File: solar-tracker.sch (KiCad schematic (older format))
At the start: 21 parts, among them J1 LDR1, J2 LDR2, J3 Motor, J4 Power, Q1 TIP41C, Q2 TIP41C, Q3 TIP42C, Q4 TIP42C, U1 LM324

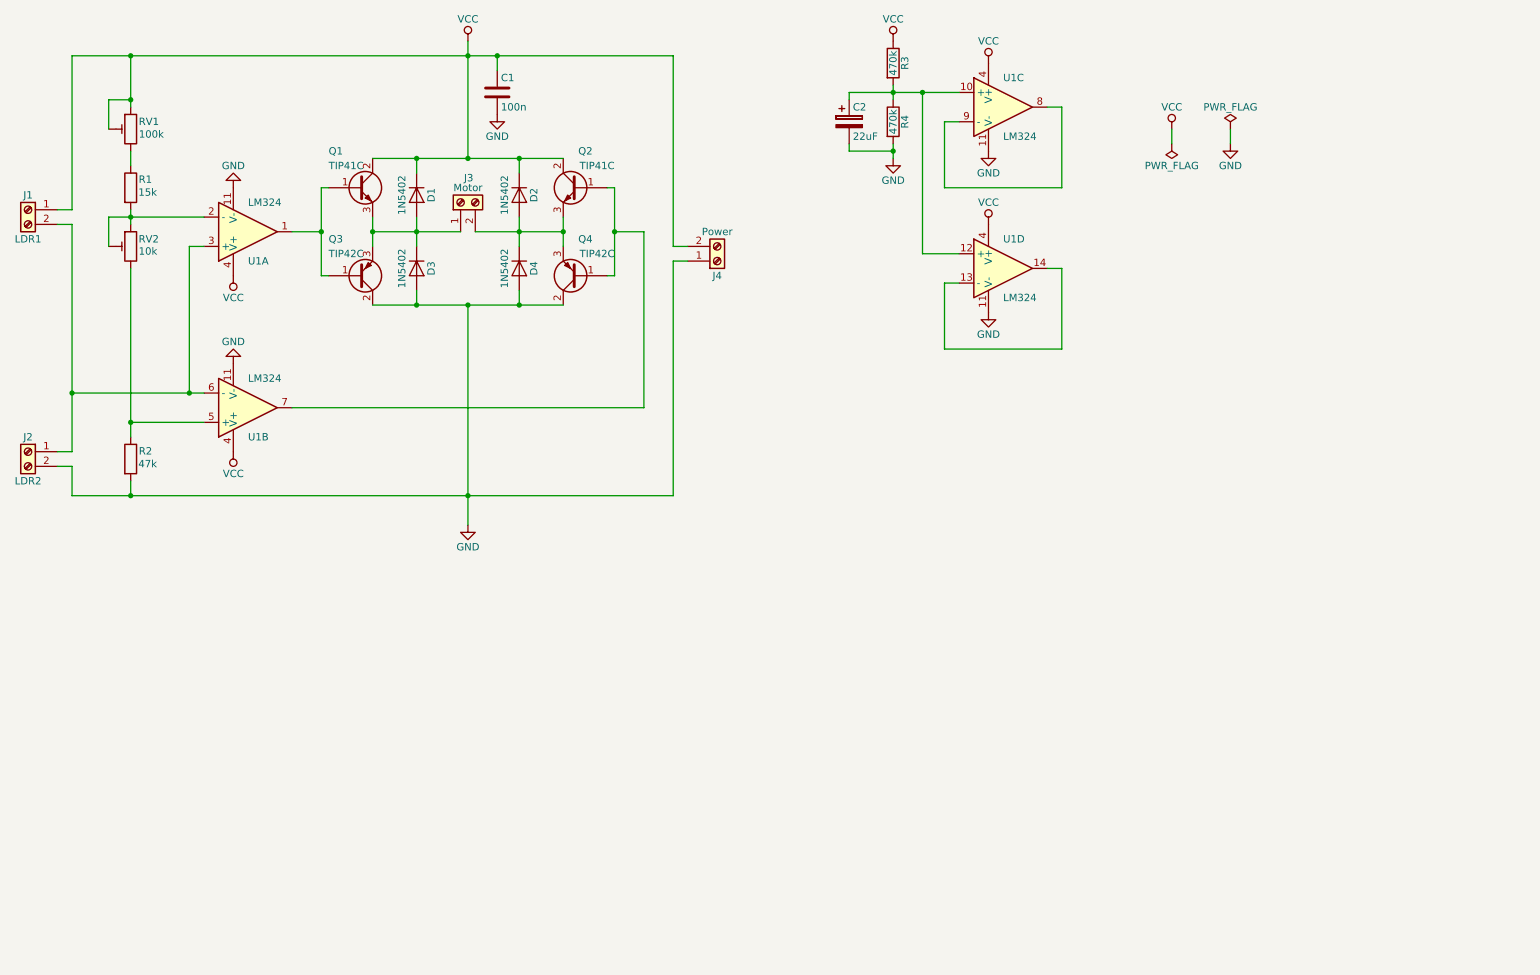
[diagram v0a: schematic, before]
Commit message: Update schematic and PCB to Revision B
- Add limit switches + diodes
- Vcc -> 9V
- Use JST XH connectors for photo-resistors (instead of screw terminal
  blocks)
- Add mounting holes to schematic
- Bring back the copper pour; for Toner Transfer Method one can simply
  remove it
- Add copper pour for front layer (F.Cu)
- Add +/- labels for power and motor terminal blocks

Signed-off-by: Sam Protsenko <joe.skb7@gmail.com>
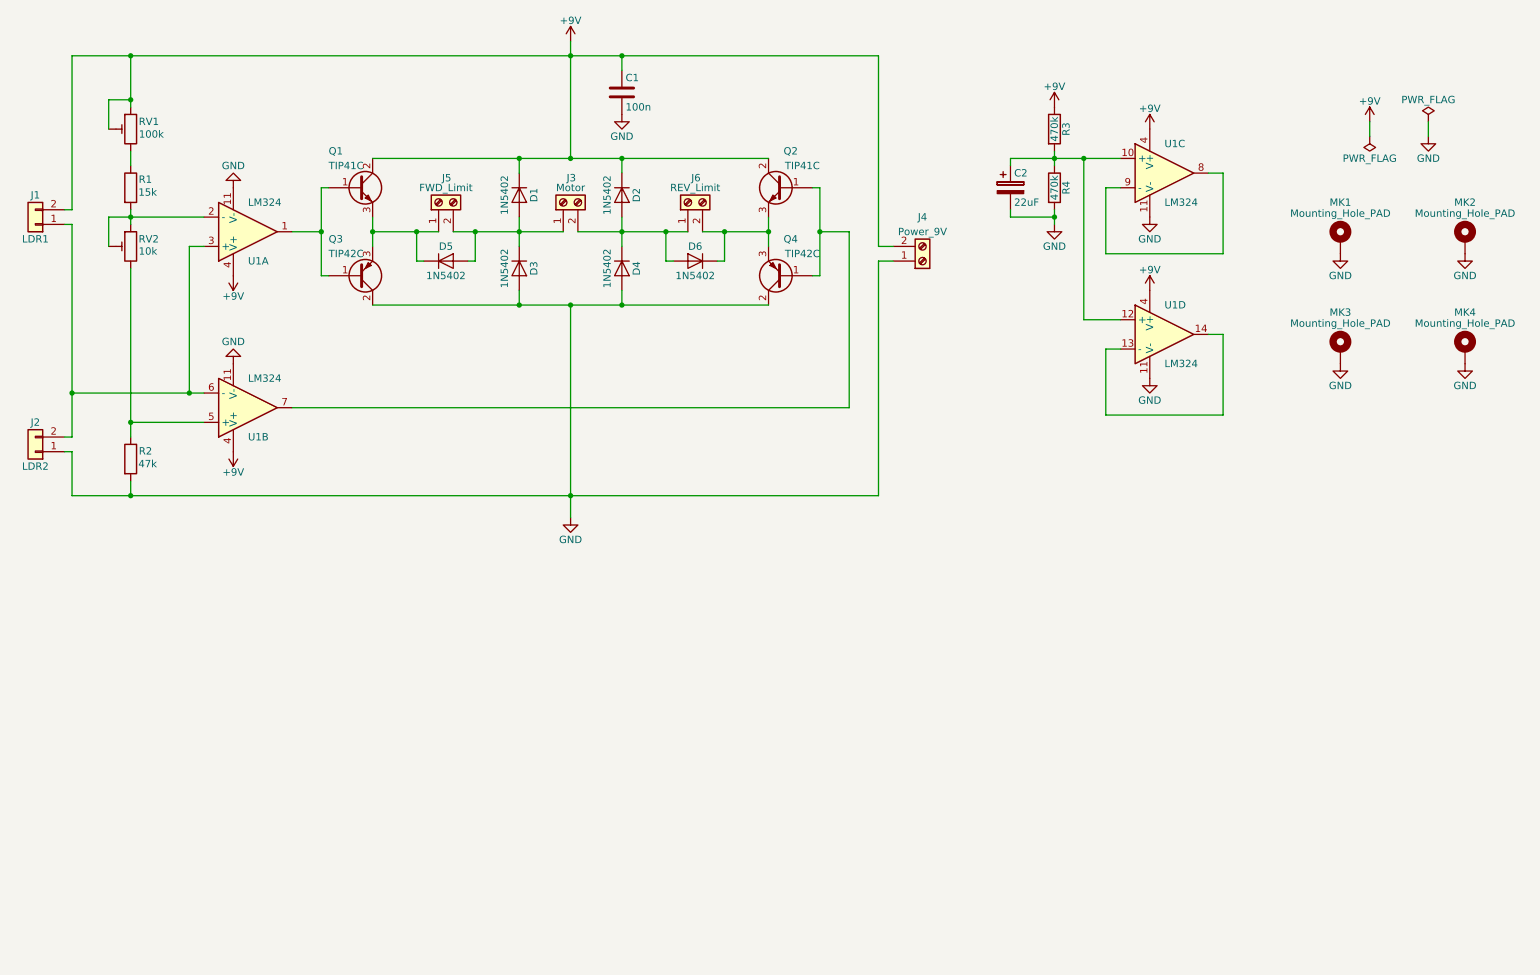
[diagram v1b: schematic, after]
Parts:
- removed J1: LDR1, Connectors_Terminal_Blocks:TerminalBlock_Pheonix_MKDS1.5-2pol, symbol Screw_Terminal_01x02
- removed J2: LDR2, Connectors_Terminal_Blocks:TerminalBlock_Pheonix_MKDS1.5-2pol, symbol Screw_Terminal_01x02
- added D5, D6: 1N5402, Diodes_THT:D_DO-201AD_P5.08mm_Vertical_KathodeUp, symbol 1N5402
- added J1: LDR1, Connectors_JST:JST_XH_B02B-XH-A_02x2.50mm_Straight, symbol Conn_01x02
- added J2: LDR2, Connectors_JST:JST_XH_B02B-XH-A_02x2.50mm_Straight, symbol Conn_01x02
- added J5: FWD_Limit, Connectors_Terminal_Blocks:TerminalBlock_Pheonix_MKDS1.5-2pol, symbol Screw_Terminal_01x02
- added J6: REV_Limit, Connectors_Terminal_Blocks:TerminalBlock_Pheonix_MKDS1.5-2pol, symbol Screw_Terminal_01x02
- added MK1, MK2, MK3, MK4: Mounting_Hole_PAD, Mounting_Holes:MountingHole_3.2mm_M3_Pad, symbol Mounting_Hole_PAD
- J4: value Power -> Power_9V
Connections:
- net GND: now also J2.1 (Pin_1), MK1.1, MK2.1, MK3.1, MK4.1
- net at U1.3 (+), U1.6 (-): now also J1.1 (Pin_1), J2.2 (Pin_2)
- net at D1.2 (A), D3.1 (K), J3.1 (Pin_1): now also D5.2 (A), J5.2 (Pin_2); no longer Q1.3 (E), Q3.3 (E)
- net at D2.2 (A), D4.1 (K), J3.2 (Pin_2): now also D6.2 (A), J6.1 (Pin_1); no longer Q2.3 (E), Q4.3 (E)
- net VCC renamed +9V
- net +9V: now also J1.2 (Pin_2)
- new net: D5.1 (K), J5.1 (Pin_1), Q1.3 (E), Q3.3 (E)
- new net: D6.1 (K), J6.2 (Pin_2), Q2.3 (E), Q4.3 (E)
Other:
- moved on the sheet: C1, C2, D1, D2, D3, D4, J3, J4, Q2, Q4, R3, R4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

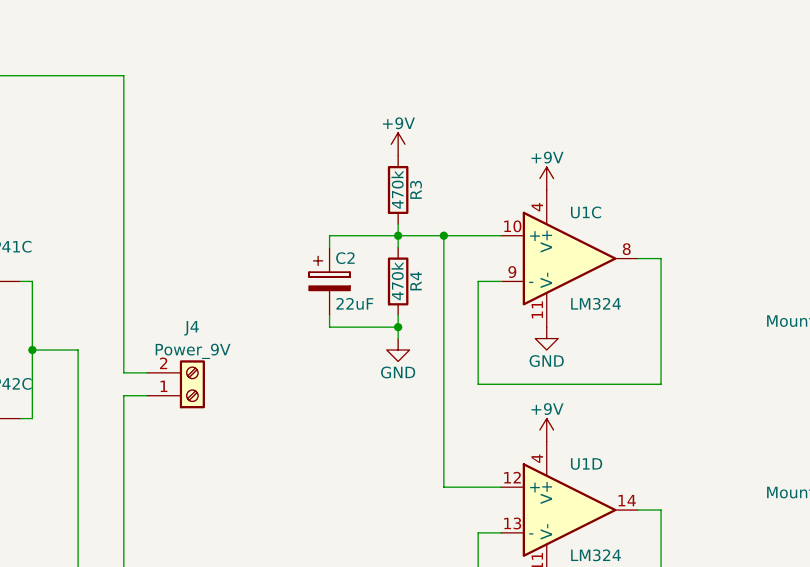
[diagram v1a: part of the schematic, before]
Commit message: Remove electrolytic capacitor
It's slowing really slow, preventing to measure final voltage on unused
OPAMPs terminals.

Signed-off-by: Sam Protsenko <joe.skb7@gmail.com>
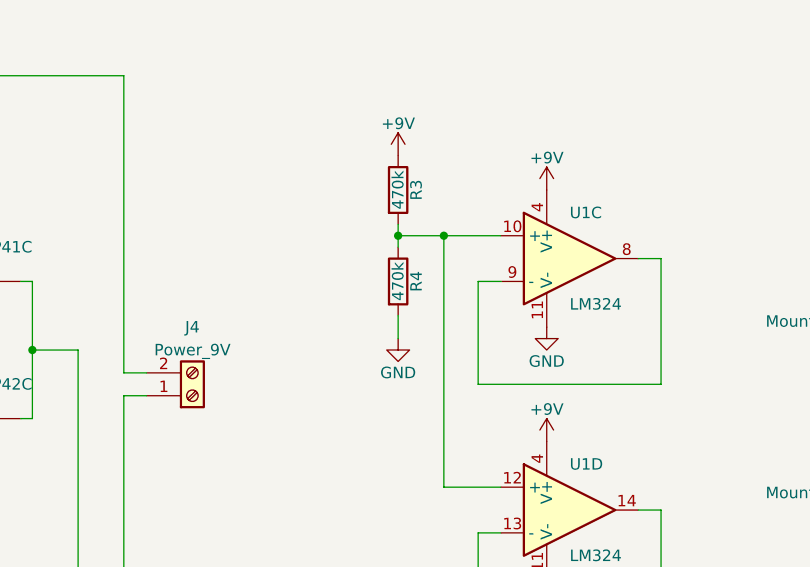
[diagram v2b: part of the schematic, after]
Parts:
- removed C2: 22uF, Capacitors_THT:CP_Radial_D8.0mm_P3.50mm, symbol CP
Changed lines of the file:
@@
 Sheet 1 1
 Title "Solar tracker"
-Date "2017-12-02"
-Rev "B"
+Date "2018-04-07"
+Rev "C"
 Comp "Dark Engineering Initiative"
 Comment1 "Author: Sam Protsenko <joe.skb7@gmail.com>"
@@
 $EndComp
 $Comp
-L CP C2
-U 1 1 5A19AAD7
-P 7500 1800
-F 0 "C2" H 7525 1900 50  0000 L CNN
-F 1 "22uF" H 7525 1700 50  0000 L CNN
-F 2 "Capacitors_THT:CP_Radial_D8.0mm_P3.50mm" H 7538 1650 50  0001 C CNN
-F 3 "" H 7500 1800 50  0001 C CNN
-	1    7500 1800
-	1    0    0    -1
-$EndComp
-$Comp
 L GND #PWR05
 U 1 1 5A19D40A
@@
 Wire Wire Line
 	7800 1950 7800 2050
-Connection ~ 7800 2000
 Wire Wire Line
 	7800 1550 7800 1650
@@
 Wire Wire Line
 	8000 2700 8000 1600
-Wire Wire Line
-	7500 1600 8250 1600
 Connection ~ 8000 1600
 Wire Wire Line
@@
 Connection ~ 1100 3200
 Connection ~ 1900 3200
-Wire Wire Line
-	7500 2000 7800 2000
-Wire Wire Line
-	7500 1600 7500 1650
-Wire Wire Line
-	7500 2000 7500 1950
 Wire Wire Line
 	1500 3900 1500 3800
@@
 	1    0    0    -1
 $EndComp
+Wire Wire Line
+	7800 1600 8250 1600
 $EndSCHEMATC

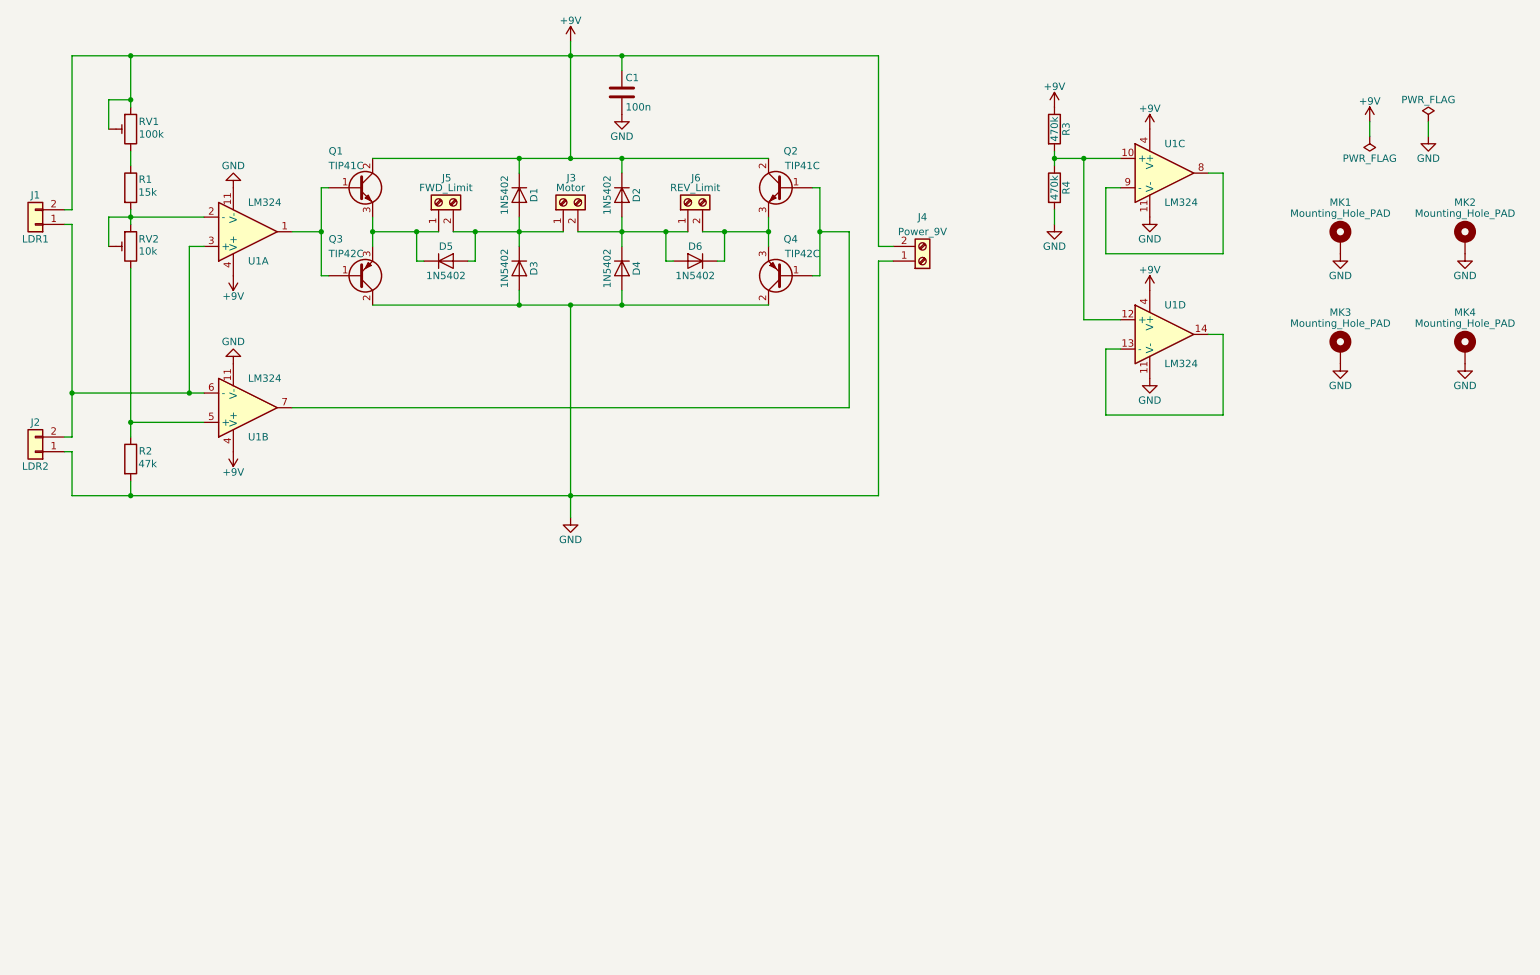
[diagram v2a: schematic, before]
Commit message: schematic: Add means to separate control/power parts
Add 0-Ohm R10, R11 so that user is able to separate control board from
power board for debugging purposes.

Signed-off-by: Sam Protsenko <joe.skb7@gmail.com>
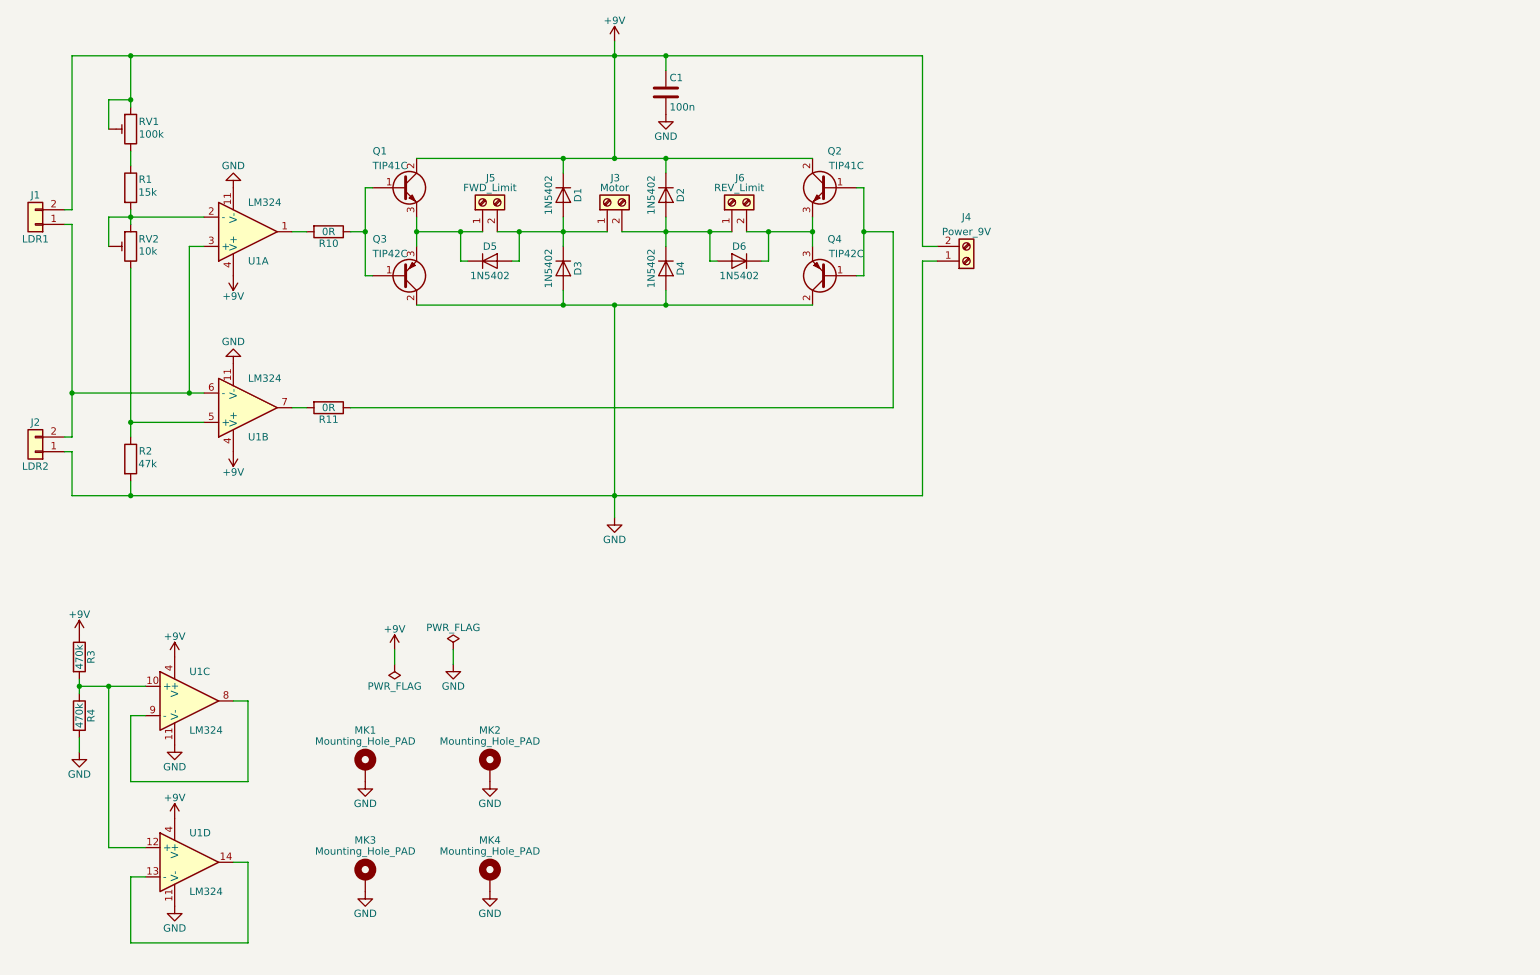
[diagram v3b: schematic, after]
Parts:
- added R10, R11: 0R, Resistors_THT:R_Axial_DIN0207_L6.3mm_D2.5mm_P10.16mm_Horizontal, symbol R
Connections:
- net at Q1.1 (B), Q3.1 (B): now also R10.1; no longer U1.1
- net at Q2.1 (B), Q4.1 (B): now also R11.1; no longer U1.7
- new net: R10.2, U1.1
- new net: R11.2, U1.7
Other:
- moved on the sheet: C1, D1, D2, D3, D4, D5, D6, J3, J4, J5, J6, MK1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

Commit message: Migrate to KiCad 5.0
Signed-off-by: Sam Protsenko <joe.skb7@gmail.com>
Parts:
- removed U1: LM324, Housings_DIP:DIP-14_W7.62mm, symbol LM324
- added U1: LM324, Package_DIP:DIP-14_W7.62mm, symbol Amplifier_Operational:LM324
- C1: footprint Capacitors_THT:C_Disc_D5.0mm_W2.5mm_P5.00mm -> Capacitor_THT:C_Disc_D5.0mm_W2.5mm_P5.00mm; symbol C -> Device:C
- D1, D2, D3, D4: footprint Diodes_THT:D_DO-201AD_P15.24mm_Horizontal -> Diode_THT:D_DO-201AD_P15.24mm_Horizontal; symbol 1N5402 -> Diode:1N5402
- D5, D6: footprint Diodes_THT:D_DO-201AD_P5.08mm_Vertical_KathodeUp -> Diode_THT:D_DO-201AD_P5.08mm_Vertical_KathodeUp; symbol 1N5402 -> Diode:1N5402
- J1, J2: footprint Connectors_JST:JST_XH_B02B-XH-A_02x2.50mm_Straight -> Connector_JST:JST_XH_B02B-XH-A_1x02_P2.50mm_Vertical; symbol Conn_01x02 -> Connector_Generic:Conn_01x02
- J3, J4, J5, J6: footprint Connectors_Terminal_Blocks:TerminalBlock_Pheonix_MKDS1.5-2pol -> TerminalBlock_Phoenix:TerminalBlock_Phoenix_MKDS-1,5-2_1x02_P5.00mm_Horizontal; symbol Screw_Terminal_01x02 -> Connector:Screw_Terminal_01x02
- MK1, MK2, MK3, MK4: footprint Mounting_Holes:MountingHole_3.2mm_M3_Pad -> MountingHole:MountingHole_3.2mm_M3_Pad; symbol Mounting_Hole_PAD -> Mechanical:MountingHole_Pad
- Q1, Q2: footprint TO_SOT_Packages_THT:TO-220_Vertical -> Package_TO_SOT_THT:TO-220-3_Vertical; symbol TIP41C -> Transistor_BJT:TIP41C
- Q3, Q4: footprint TO_SOT_Packages_THT:TO-220_Vertical -> Package_TO_SOT_THT:TO-220-3_Vertical; symbol TIP42C -> Transistor_BJT:TIP42C
- R1, R10, R11, R2, R3, R4: footprint Resistors_THT:R_Axial_DIN0207_L6.3mm_D2.5mm_P10.16mm_Horizontal -> Resistor_THT:R_Axial_DIN0207_L6.3mm_D2.5mm_P10.16mm_Horizontal; symbol R -> Device:R
- RV1, RV2: footprint Potentiometers:Potentiometer_Trimmer_Bourns_3266W -> Potentiometer_THT:Potentiometer_Bourns_3266W_Vertical; symbol POT_TRIM -> Device:R_POT_TRIM
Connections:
- wire segments 80 -> 113
